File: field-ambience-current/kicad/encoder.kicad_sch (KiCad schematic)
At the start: 24 parts

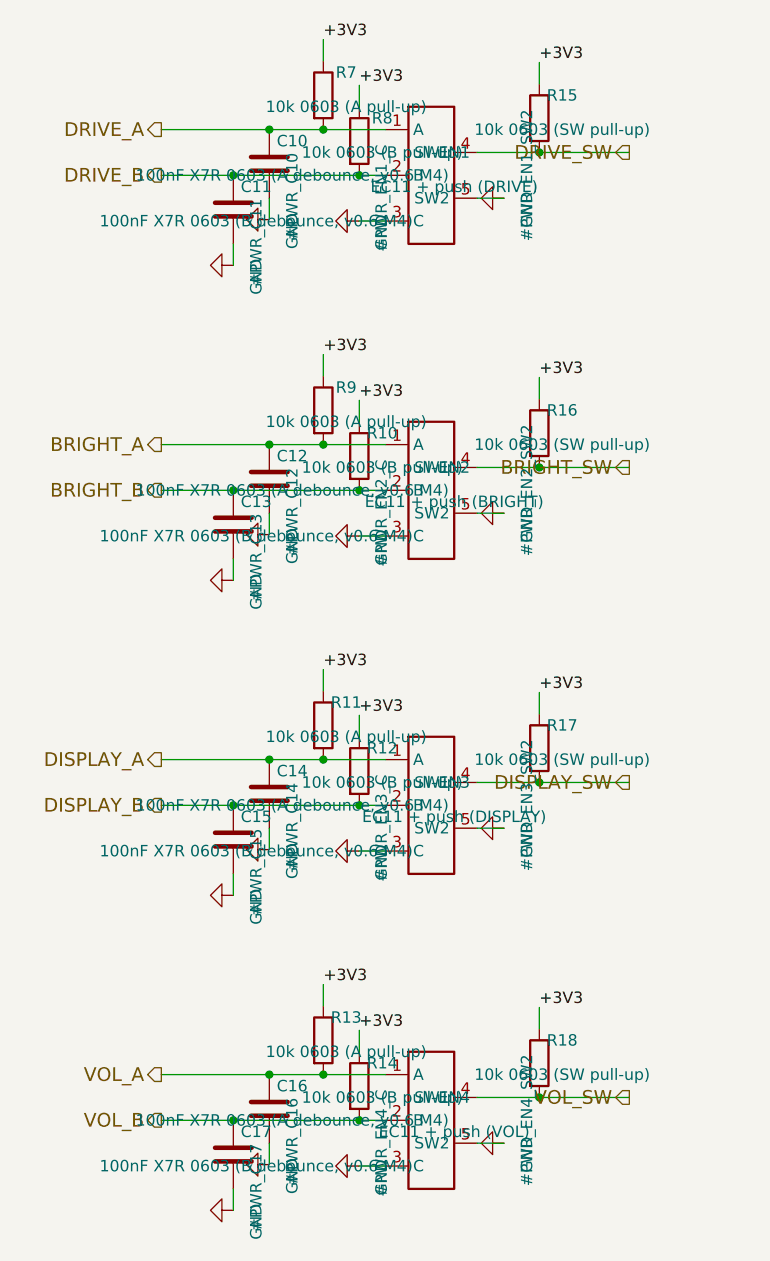
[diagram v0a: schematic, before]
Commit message: pcb+fw(r18.14): Komponenten-Definition — 3D-Lib, 2 kritische BOM-Fixes, Encoder-Strategie (ADR-0012), Cell-Keys Magnetic-Hall (ADR-0013)
User-Direktive: Komponenten vor Layout definieren, 3D-Daten zu allem, Cells
wie HiChord mit langen Caps + Stabilizern, Encoder-Split + smooth + gleich
hoch + flach (Kick75), Encoder-UX-Bug fixen.

🔴 Kritische BOM-Fixes (via 3D-CAD-Abruf entdeckt):
- USB-C: C165935 war ein STF18N65M5-MOSFET (TO-220F-3)! Korrekt: C283540
  (TYPE-C-31-M-17, LCSC-verifiziert). Falsch seit r18.10.
- SW_BOOT: C720477 ist XUNPU TS-1088-AR02016 (nicht TS-1185A-C-A);
  FP von generisch TL3342 auf EasyEDA-verifiziertes SW_TS1088_SMD.

3D-STEP-Library:
- kicad/libraries/field_ambience.3dshapes/ — 9 Z-/Panel-kritische Modelle
- mechanical/3d_models/MANIFEST.md — Inventar, Höhen, Regenerier-Kommando

ADR-0012 Encoder-Strategie:
- EN3 (Display) einziger mit Push+Detents; EN1/2/4 = EC11E183440C smooth
  (ohne Rastung/Anschlag/Switch). Alle 4 = EC11E THT, gleiche Schaftlänge
  = gleich hoch, Ziel 20-22mm statt 24.5mm (EC11J-STEP-Beleg), Kick75-flach.
- EC11J SMD retired (NRND + zu hoch + Half-Step-Mismatch). FP-Verify: 0 offen.

Encoder-UX-Fix („zwei Klicks für 1%"):
- Bench-Encoder rastet jede halbe Quadratur-Periode → ENC_HALF_STEP Default=1
  (display_hw_test.c), Host-Test pinnt Full-Cycle-Modus explizit.
- encoders.c: per-Encoder substeps (Display 4, Smooth 2) + has_sw-Flag.
- 12/12 Test-Suiten PASS.

ADR-0013 Cell-Keys (ersetzt FSR aus ADR-0006):
- Gateron-LP-Magnetic-Switches (HiChord-Feel) + linearer Hall-Sensor pro
  Cell → Velocity = dPos/dt, Aftertouch firmware-offen. ADC-Pins unverändert.
- Lange Caps ≥2u mit LP-Stabilizern (Spacebar-Prinzip: Switch mittig,
  Support links/rechts).
- Schematic: J_CELL 1×2-FSR-Teiler → 1×3-Hall-Site + 1k-Serien-RC.
- Sensor-Kandidaten DRV5056A4/SS49E mit explizitem PINOUT-VERIFY (AP7361-Lektion).

Modifier-Buttons: SPEC stellt explizit klar — alle 5 identisch, momentary,
Latch-Zustand nur über LEDs (ADR-0008).

Scores: F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
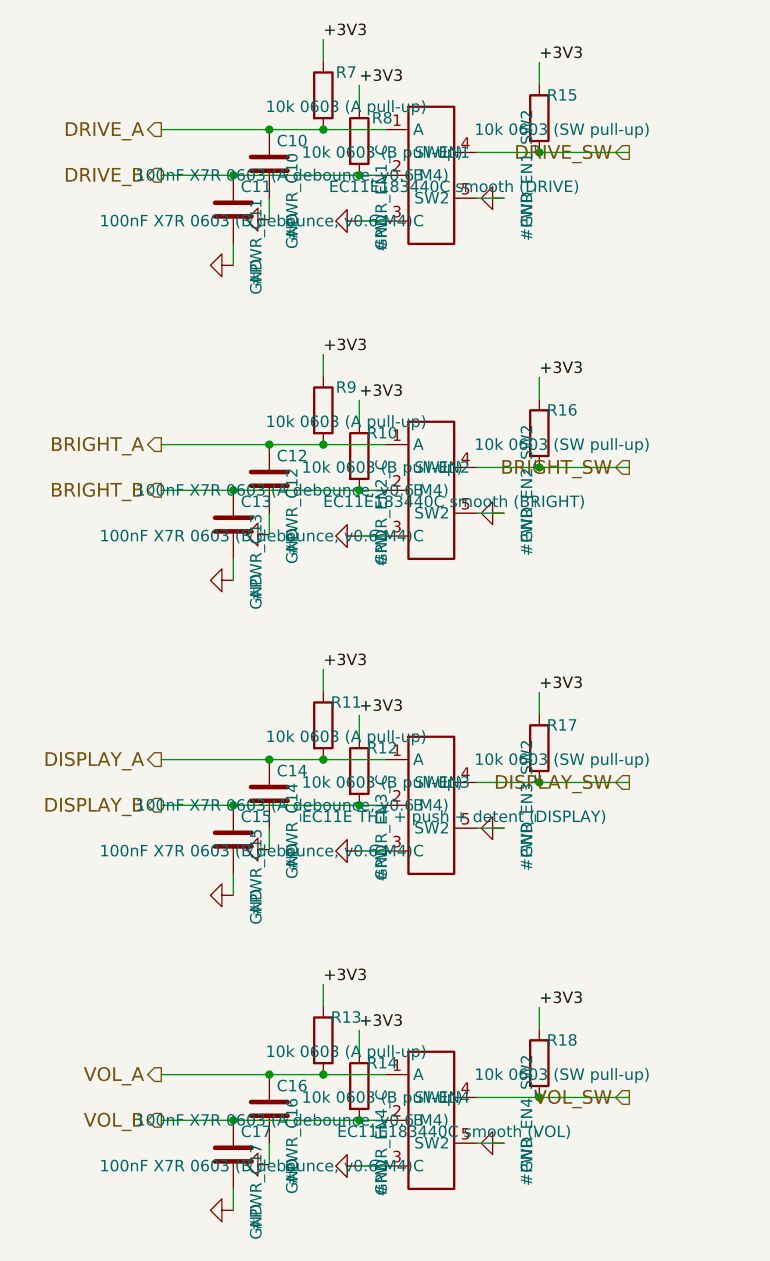
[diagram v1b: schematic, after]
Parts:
- EN1: value EC11 + push (DRIVE) -> EC11E183440C smooth (DRIVE); footprint field_ambience:RotaryEncoder_ALPS_EC11J_SMD -> Rotary_Encoder:RotaryEncoder_Alps_EC11E-Switch_Vertical_H20mm; FP_DRAFT field_ambience:RotaryEncoder_ALPS_EC11J_SMD ist ein DRAFT-F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 -> (none); FP_NOTE (none) -> Rotary_Encoder:RotaryEncoder_Alps_EC11E-Switch_Vertical_H20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; Height (none) -> Body ~7mm + Schaft (einheitliche Länge für alle 4 wählen; Z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; LCSC C209762 -> TBD-VERIFY (Original-ALPS auf LCSC prüfen, sonst Mouser/Dig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; MPN EC11J1525402 -> EC11E183440C (18 Puls, OHNE Detent, OHNE Switch); Package SMD, 15 pulses / 30 detents, push switch -> THT EC11E, vertikal, glatt drehend (kein Anschlag, kein Det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; Status NRND (ALPS marks as Not Recommended For New Designs) — Prot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 -> (none); Variant (none) -> Parameter-Encoder ohne Push: SW1/SW2-Löcher bleiben leer (V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
- EN2: value EC11 + push (BRIGHT) -> EC11E183440C smooth (BRIGHT); footprint field_ambience:RotaryEncoder_ALPS_EC11J_SMD -> Rotary_Encoder:RotaryEncoder_Alps_EC11E-Switch_Vertical_H20mm; FP_DRAFT field_ambience:RotaryEncoder_ALPS_EC11J_SMD ist ein DRAFT-F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 -> (none); FP_NOTE (none) -> Rotary_Encoder:RotaryEncoder_Alps_EC11E-Switch_Vertical_H20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; Height (none) -> Body ~7mm + Schaft (einheitliche Länge für alle 4 wählen; Z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; LCSC C209762 -> TBD-VERIFY (Original-ALPS auf LCSC prüfen, sonst Mouser/Dig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; MPN EC11J1525402 -> EC11E183440C (18 Puls, OHNE Detent, OHNE Switch); Package SMD, 15 pulses / 30 detents, push switch -> THT EC11E, vertikal, glatt drehend (kein Anschlag, kein Det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; Status NRND (ALPS marks as Not Recommended For New Designs) — Prot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 -> (none); Variant (none) -> Parameter-Encoder ohne Push: SW1/SW2-Löcher bleiben leer (V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
- EN3: value EC11 + push (DISPLAY) -> EC11E THT + push + detent (DISPLAY); footprint field_ambience:RotaryEncoder_ALPS_EC11J_SMD -> Rotary_Encoder:RotaryEncoder_Alps_EC11E-Switch_Vertical_H20mm; FP_DRAFT field_ambience:RotaryEncoder_ALPS_EC11J_SMD ist ein DRAFT-F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 -> (none); FP_NOTE (none) -> Rotary_Encoder:RotaryEncoder_Alps_EC11E-Switch_Vertical_H20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; Height (none) -> Body ~7mm + Schaft (einheitliche Länge für alle 4 wählen; Z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; LCSC C209762 -> TBD-VERIFY (Original-ALPS auf LCSC prüfen, sonst Mouser/Dig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; MPN EC11J1525402 -> ALPS EC11E-Serie, 15 Puls / 30 Detent, mit Push-Switch — ex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; Package SMD, 15 pulses / 30 detents, push switch -> THT EC11E, vertikal. Detents gewollt: Menü-Navigation 1 Ras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; Status NRND (ALPS marks as Not Recommended For New Designs) — Prot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 -> (none); Variant (none) -> DISPLAY-Encoder = einziger mit Push + Rastung (ADR-0012)
- EN4: value EC11 + push (VOL) -> EC11E183440C smooth (VOL); footprint field_ambience:RotaryEncoder_ALPS_EC11J_SMD -> Rotary_Encoder:RotaryEncoder_Alps_EC11E-Switch_Vertical_H20mm; FP_DRAFT field_ambience:RotaryEncoder_ALPS_EC11J_SMD ist ein DRAFT-F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 -> (none); FP_NOTE (none) -> Rotary_Encoder:RotaryEncoder_Alps_EC11E-Switch_Vertical_H20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; Height (none) -> Body ~7mm + Schaft (einheitliche Länge für alle 4 wählen; Z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; LCSC C209762 -> TBD-VERIFY (Original-ALPS auf LCSC prüfen, sonst Mouser/Dig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; MPN EC11J1525402 -> EC11E183440C (18 Puls, OHNE Detent, OHNE Switch); Package SMD, 15 pulses / 30 detents, push switch -> THT EC11E, vertikal, glatt drehend (kein Anschlag, kein Det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; Status NRND (ALPS marks as Not Recommended For New Designs) — Prot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 -> (none); Variant (none) -> Parameter-Encoder ohne Push: SW1/SW2-Löcher bleiben leer (V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

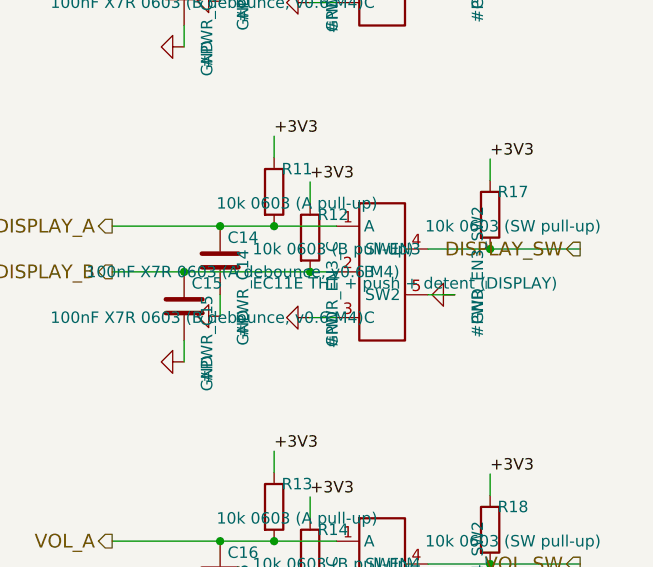
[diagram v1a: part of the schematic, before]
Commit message: pcb(r18.14b): Komponenten-IDs verifiziert — EC11E + DRV5056
Drei verbleibende TBD-VERIFY-Punkte aus r18.14a geschlossen:

- EN3 Display: EC11E18244AU = C202365 (ALPS, 18P/36D + push, LCSC in stock)
- EN1/2/4 Smooth: EC11E183440C = C370986 (ALPS, 18P/no-detent + push,
  selbe Bauform → alle 4 gleich hoch verifiziert)
- Hall-Sensor: DRV5056A4QDBZR = C2152902 (TI SOT-23, 3.3V ratiometrisch)

DRV5056-Pinout aus TI-DS Table 4-1 verifiziert (statt geraten):
SOT-23: Pin 1=VCC, Pin 2=OUT, Pin 3=GND — matched 1:1 zur 1×3-Site.
TO-92-Variante (Prototyp) hat ABWEICHENDE Belegung (1=VCC/2=GND/3=OUT) —
Beine für Breadboard swappen.

Generator + SPEC §4 mit echten LCSC-IDs + Datasheet-URLs versorgt.
PROJECT_QUALITY BOM 8.5→9.

Offen für 10/10 BOM: Gateron-LP-Switches (Keyboard-Markt, kein LCSC),
470µF/16V Polymer 7343 (Web-Suche unzureichend, JLCPCB-GUI nötig),
220µF/10V MLCC 1210 (Samsung CL32A227MQVNNNE=C400951 ist 6.3V,
Headroom an 5V-PVDD knapp — 10V-Variante in Phase 6 final wählen).

https://claude.ai/code/session_01K5kLTFpDCCoYwx2dq6RkAv
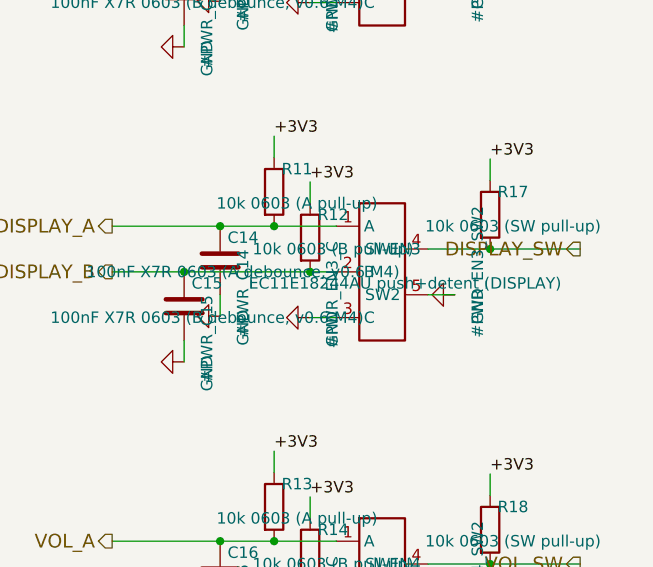
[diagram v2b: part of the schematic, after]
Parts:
- EN1, EN2, EN4: FP_NOTE Rotary_Encoder:RotaryEncoder_Alps_EC11E-Switch_Vertical_H20mm = KiCad-Standard-Lib (fab-erprobt). Land-Pattern für alle EC11E-Schafthöhen identisch; H20mm betrifft nur das 3D-Modell. Smooth-Variante nutzt dasselbe FP — S1/S2-Löcher bleiben leer. -> Rotary_Encoder:RotaryEncoder_Alps_EC11E-Switch_Vertical_H20mm — KiCad-Standard-Lib, fab-erprobt. Identisches Land-Pattern für beide Varianten (Push-Pins immer da, im Smooth-Fall mechanisch ungenutzt). r18.14: LCSC-IDs verifiziert.; Height Body ~7mm + Schaft (einheitliche Länge für alle 4 wählen; Z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 -> Beide Varianten gleiche Bauform: Body 11.7×12.0×4.5 mm + 20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; LCSC TBD-VERIFY (Original-ALPS auf LCSC prüfen, sonst Mouser/Dig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 -> C370986; MPN EC11E183440C (18 Puls, OHNE Detent, OHNE Switch) -> EC11E183440C (ALPS EC11E, 18 Pulse, OHNE Detent, MIT Push-S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; Package THT EC11E, vertikal, glatt drehend (kein Anschlag, kein Det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 -> THT EC11E vertikal, Shaft 20mm — Parameter-Encoder: glatt d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; Variant Parameter-Encoder ohne Push: SW1/SW2-Löcher bleiben leer (V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 -> Parameter-Encoder: smooth Drehung; Firmware nutzt nur A/B
- EN3: value EC11E THT + push + detent (DISPLAY) -> EC11E18244AU push+detent (DISPLAY); FP_NOTE Rotary_Encoder:RotaryEncoder_Alps_EC11E-Switch_Vertical_H20mm = KiCad-Standard-Lib (fab-erprobt). Land-Pattern für alle EC11E-Schafthöhen identisch; H20mm betrifft nur das 3D-Modell. Smooth-Variante nutzt dasselbe FP — S1/S2-Löcher bleiben leer. -> Rotary_Encoder:RotaryEncoder_Alps_EC11E-Switch_Vertical_H20mm — KiCad-Standard-Lib, fab-erprobt. Identisches Land-Pattern für beide Varianten (Push-Pins immer da, im Smooth-Fall mechanisch ungenutzt). r18.14: LCSC-IDs verifiziert.; Height Body ~7mm + Schaft (einheitliche Länge für alle 4 wählen; Z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 -> Beide Varianten gleiche Bauform: Body 11.7×12.0×4.5 mm + 20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; LCSC TBD-VERIFY (Original-ALPS auf LCSC prüfen, sonst Mouser/Dig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 -> C202365; MPN ALPS EC11E-Serie, 15 Puls / 30 Detent, mit Push-Switch — ex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 -> EC11E18244AU (ALPS EC11E, 18 Pulse, 36 Detents, mit Push-Sw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; Package THT EC11E, vertikal. Detents gewollt: Menü-Navigation 1 Ras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 -> THT EC11E vertikal, Shaft 20mm flat — Display-Encoder: 1 Ra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; Variant DISPLAY-Encoder = einziger mit Push + Rastung (ADR-0012) -> DISPLAY-Encoder = einziger mit Push + Rastung

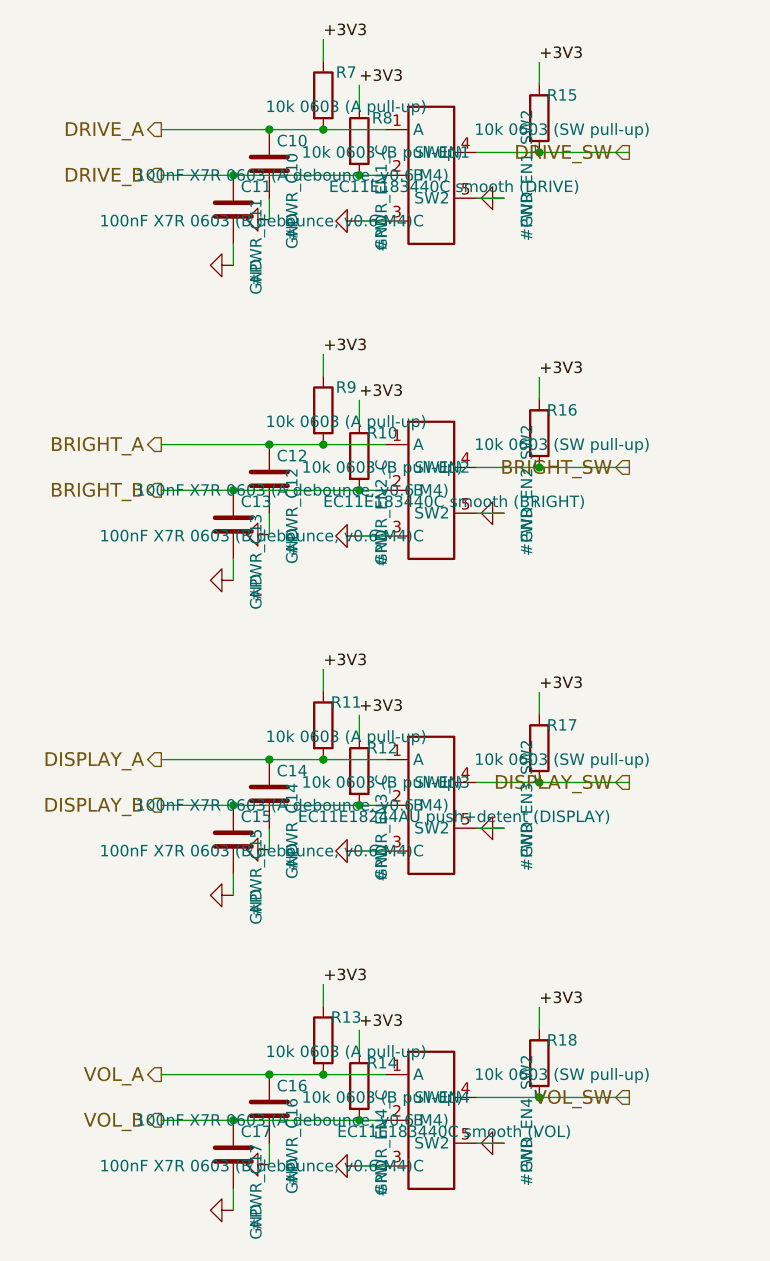
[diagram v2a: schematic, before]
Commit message: pcb(r18.22): User-Verifikation — Encoder-NRND-Pivot + Display-Qualitäts-Pivot
User: "Er ist nochmal alles gegen checken und verifizieren. Glaube die Encoder
waren markiert als NRND? Und das Display darf nicht schlecht sein."
→ Beide Punkte berechtigt, beide gefixt.

🔴 HIGH — Encoder NRND-Pivot (3 von 4 betroffen)
- EC11E183440C (C370986, Smooth × 3) = NRND bestätigt (Octopart, RS, ALPS-
  Hersteller-Seite). 19-Wochen-Lead bei TTI.
- EC11E1834403 (C361165, obvious-Kandidat) = AUCH NRND.
- ALPS hat die gesamte "EC11E 0-Detent + Push-Switch"-Familie phased out.
- Pivot: alle 4 = EC11E18244AU (active, C202365, ~3052 LCSC-Stock).
  UX bleibt identisch (Firmware-Acceleration macht langsam=1%/Klick,
  schnell=×8 — die Detents waren die ursprüngliche UX-Lösung).
  Bonus: alle 4 identisch → Lagerhaltung simpel.

🟠 HIGH — Display-Qualitäts-Pivot (r18.21-Korrektur)
- Bare-AliExpress nutzt dasselbe Panel wie Adafruit, aber kein Level-Shifter,
  kein QC, DOA-Lotterie, FFC-Roulette.
- Adafruit $15 zahlt für Features, die wir bei 3V3-STM32 nicht brauchen.
- Pivot: Waveshare 1.9in ST7789V2 (~$11-13, PiHut/Waveshare/Amazon) — gleiches
  Panel + branded QC + Level-Shifter + dokumentiert.
- Aufpreis $40 für 5 Geräte für komplette Risk-Reduktion. Wert.

Lehre dokumentiert in ADR-0012: Lifecycle-Status muss aktiv verifiziert
werden, nicht nur Stock. Analog zur Pin-Count-Pflicht nach r18.19.

Verifizierung: 8/8 paren-balanced, encoder.kicad_sch hat 8× C202365 active,
3 C370986-Reste sind ausschließlich in Lifecycle-VERIFIED-Audit-Notizen.
Firmware 13/13 PASS.

Cost: r18.21 ~$405 → r18.22 ~$445/5 Geräte ($89/Stück). $40 Aufpreis,
volle Risk-Reduktion (NRND + DOA-Lotterie eliminiert).

Files: generate_kicad_project.py, encoder.kicad_sch regen, BOM_MASTER,
ADR-0012, COST_ESTIMATE, CHANGELOG.

https://claude.ai/code/session_01K5kLTFpDCCoYwx2dq6RkAv
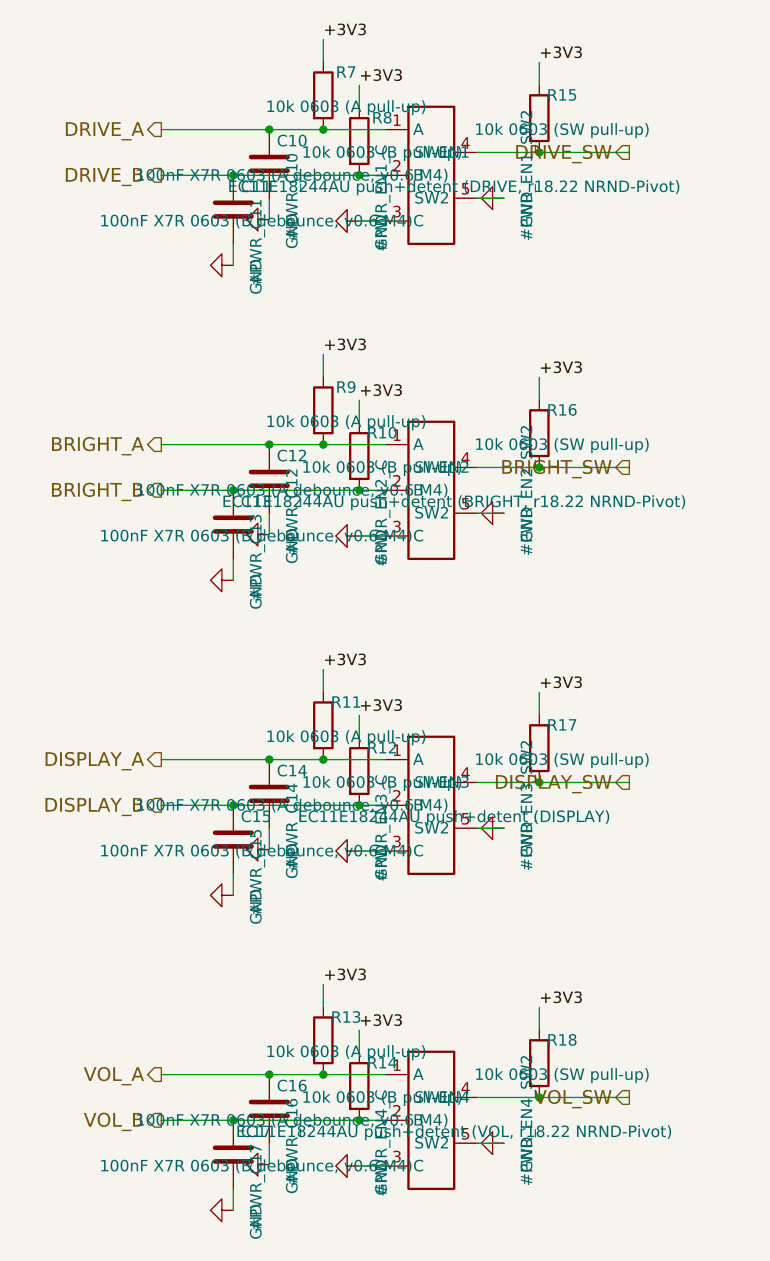
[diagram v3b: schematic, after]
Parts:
- EN1: value EC11E183440C smooth (DRIVE) -> EC11E18244AU push+detent (DRIVE, r18.22 NRND-Pivot); LCSC C370986 -> C202365; Lifecycle-VERIFIED (none) -> ALPS-Hersteller-Seite: Standard / for new designs (r18.22 v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; MPN EC11E183440C (ALPS EC11E, 18 Pulse, OHNE Detent, MIT Push-S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 -> EC11E18244AU (ALPS EC11E, 18 Pulse, 36 Detents, mit Push-Sw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; Package THT EC11E vertikal, Shaft 20mm — Parameter-Encoder: glatt d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 -> THT EC11E vertikal, Shaft 20mm flat — Parameter-Encoder (r1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; Variant Parameter-Encoder: smooth Drehung; Firmware nutzt nur A/B -> Parameter-Encoder = identisch zu Display-Encoder (r18.22 Ve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
- EN2: value EC11E183440C smooth (BRIGHT) -> EC11E18244AU push+detent (BRIGHT, r18.22 NRND-Pivot); LCSC C370986 -> C202365; Lifecycle-VERIFIED (none) -> ALPS-Hersteller-Seite: Standard / for new designs (r18.22 v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; MPN EC11E183440C (ALPS EC11E, 18 Pulse, OHNE Detent, MIT Push-S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 -> EC11E18244AU (ALPS EC11E, 18 Pulse, 36 Detents, mit Push-Sw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; Package THT EC11E vertikal, Shaft 20mm — Parameter-Encoder: glatt d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 -> THT EC11E vertikal, Shaft 20mm flat — Parameter-Encoder (r1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; Variant Parameter-Encoder: smooth Drehung; Firmware nutzt nur A/B -> Parameter-Encoder = identisch zu Display-Encoder (r18.22 Ve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
- EN4: value EC11E183440C smooth (VOL) -> EC11E18244AU push+detent (VOL, r18.22 NRND-Pivot); LCSC C370986 -> C202365; Lifecycle-VERIFIED (none) -> ALPS-Hersteller-Seite: Standard / for new designs (r18.22 v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; MPN EC11E183440C (ALPS EC11E, 18 Pulse, OHNE Detent, MIT Push-S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 -> EC11E18244AU (ALPS EC11E, 18 Pulse, 36 Detents, mit Push-Sw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; Package THT EC11E vertikal, Shaft 20mm — Parameter-Encoder: glatt d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 -> THT EC11E vertikal, Shaft 20mm flat — Parameter-Encoder (r1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; Variant Parameter-Encoder: smooth Drehung; Firmware nutzt nur A/B -> Parameter-Encoder = identisch zu Display-Encoder (r18.22 Ve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
